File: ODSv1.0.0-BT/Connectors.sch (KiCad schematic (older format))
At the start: 2 parts, among them J1 Conn_02x60_Odd_Even, J2 Conn_02x60_Odd_Even

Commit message: Associate backplane template symbols with footprints and BOM info
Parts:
- J1: MPN (none) -> FX20-120P-0.5SV15; Manufacturer (none) -> Hirose; Ordering URL (none) -> https://www.digikey.com/en/products/detail/hirose-electric-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
- J2: footprint Backplane_Connector_Hirose:Hirose_FX20_FX20-120P-0.5SV_2x60_P0.50mm_Vertical -> Backplane_Connector_Hirose:Hirose_FX20_FX20-120S-0.5SV_2x60_P0.50mm_Vertical; MPN (none) -> FX20-120S-0.5SV; Manufacturer (none) -> Hirose; Ordering URL (none) -> https://www.digikey.com/en/products/detail/hirose-electric-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
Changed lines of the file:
@@
 F 2 "Backplane_Connector_Hirose:Hirose_FX20_FX20-120P-0.5SV_2x60_P0.50mm_Vertical" H 2450 3950 50  0001 C CNN
 F 3 "https://www.hirose.com/product/document?clcode=&productname=&series=FX20&documenttype=Catalog&lang=en&documentid=D49373_en" H 2450 3950 50  0001 C CNN
+F 4 "FX20-120P-0.5SV15" H 2450 3950 50  0001 C CNN "MPN"
+F 5 "Hirose" H 2450 3950 50  0001 C CNN "Manufacturer"
+F 6 "https://www.digikey.com/en/products/detail/hirose-electric-co-ltd/FX20-120P-0-5SV15/3461671" H 2450 3950 50  0001 C CNN "Ordering URL"
 	1    2450 3950
 	1    0    0    -1
@@
 F 0 "J2" H 5500 7067 50  0000 C CNN
 F 1 "Conn_02x60_Odd_Even" H 5500 6976 50  0000 C CNN
-F 2 "Backplane_Connector_Hirose:Hirose_FX20_FX20-120P-0.5SV_2x60_P0.50mm_Vertical" H 5450 3950 50  0001 C CNN
+F 2 "Backplane_Connector_Hirose:Hirose_FX20_FX20-120S-0.5SV_2x60_P0.50mm_Vertical" H 5450 3950 50  0001 C CNN
 F 3 "https://www.hirose.com/product/document?clcode=&productname=&series=FX20&documenttype=Catalog&lang=en&documentid=D49373_en" H 5450 3950 50  0001 C CNN
+F 4 "FX20-120S-0.5SV" H 5450 3950 50  0001 C CNN "MPN"
+F 5 "Hirose" H 5450 3950 50  0001 C CNN "Manufacturer"
+F 6 "https://www.digikey.com/en/products/detail/hirose-electric-co-ltd/FX20-120S-0-5SV/3461673" H 5450 3950 50  0001 C CNN "Ordering URL"
 	1    5450 3950
 	1    0    0    -1

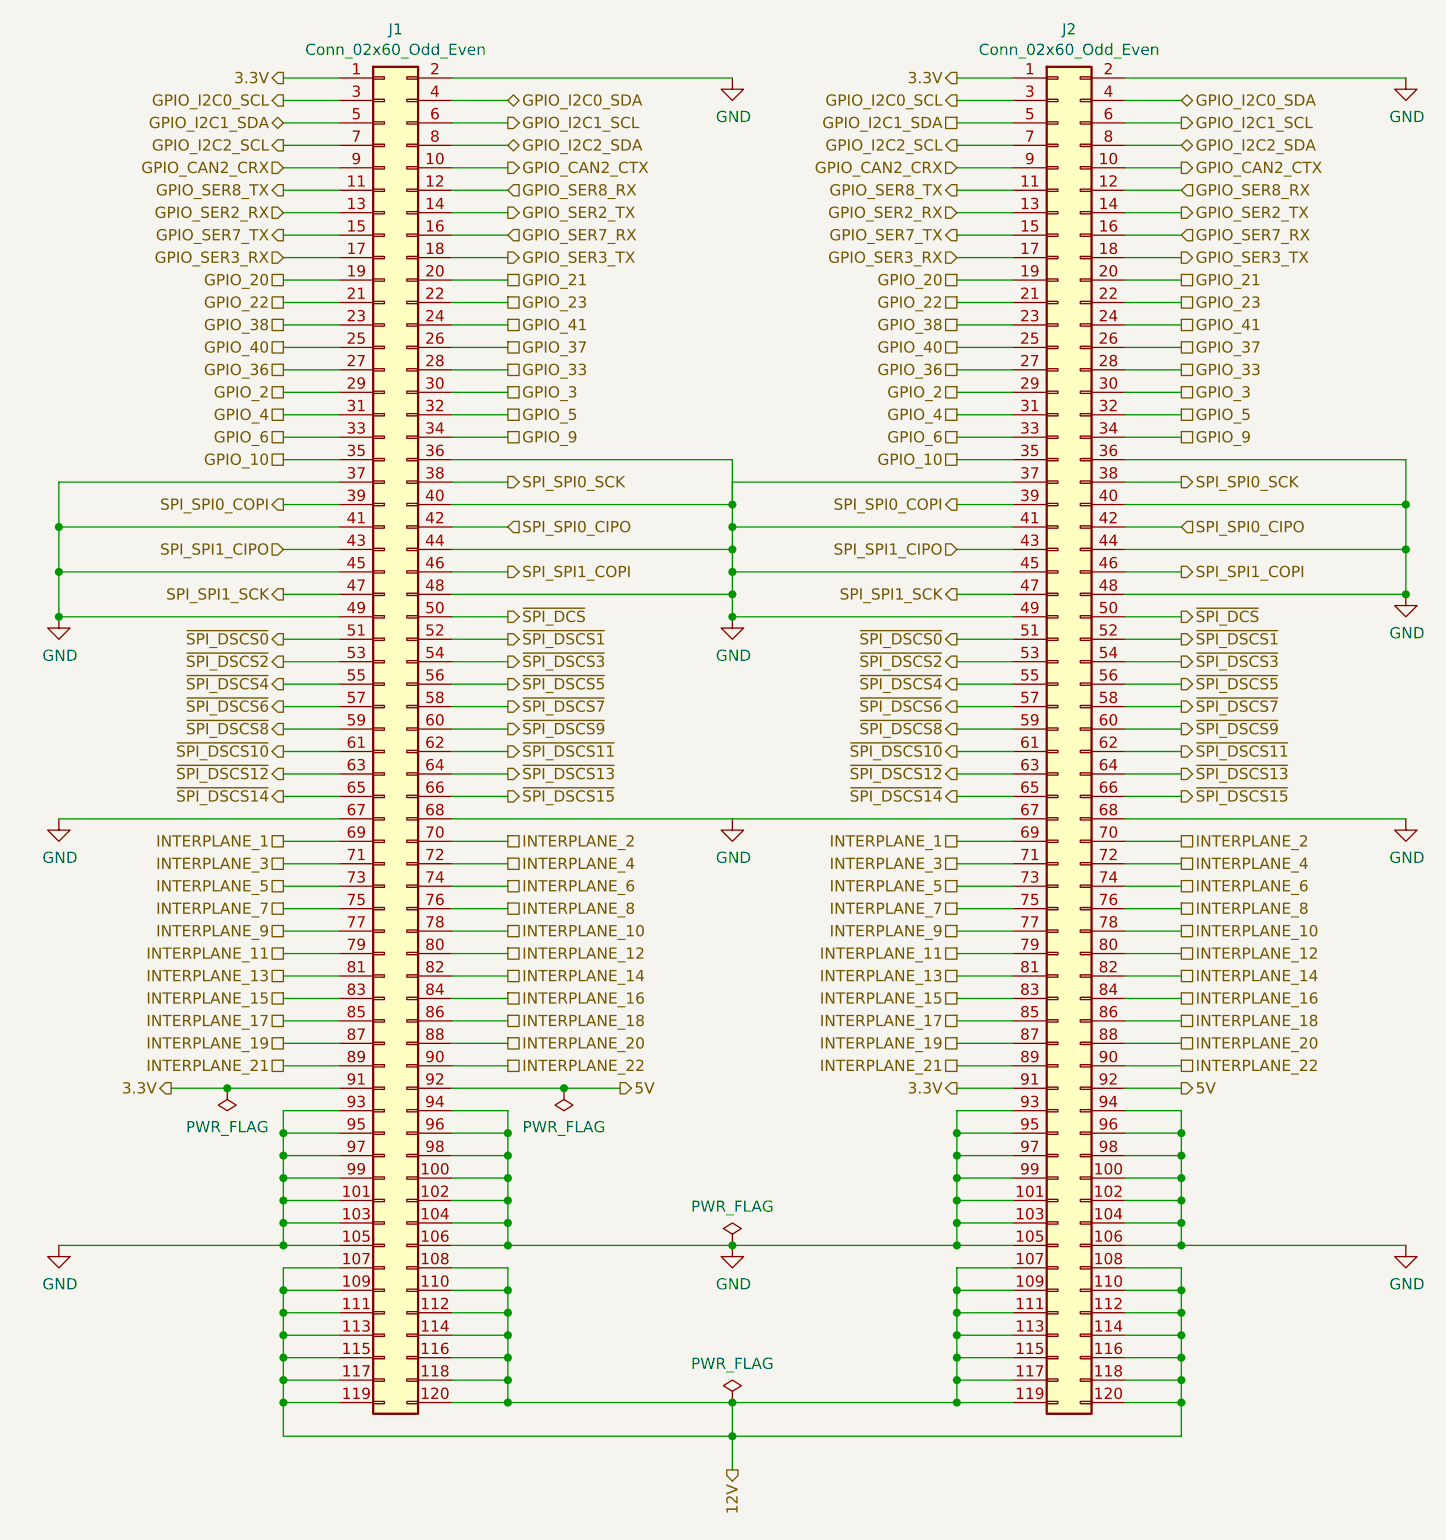
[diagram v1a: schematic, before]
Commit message: Remap pins for easier layout
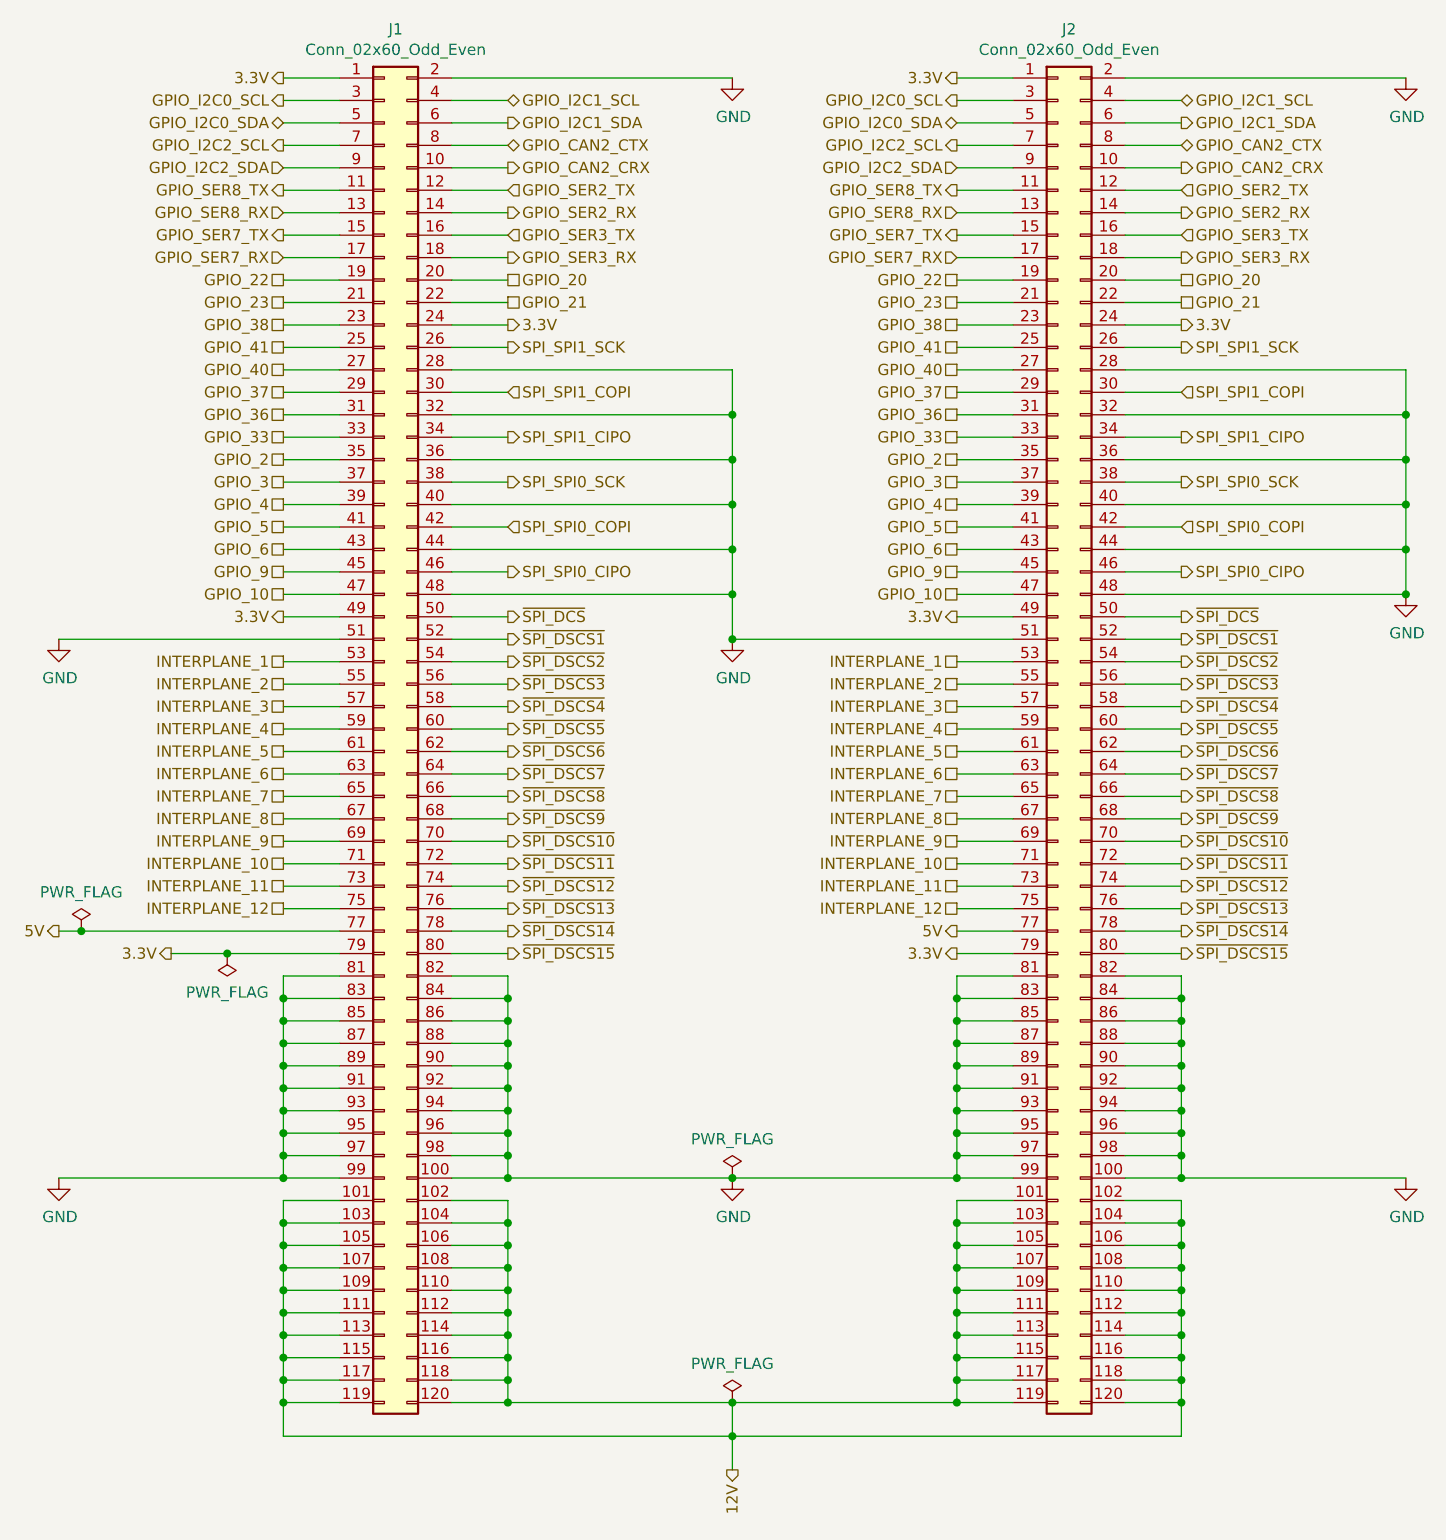
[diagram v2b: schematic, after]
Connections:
- net INTERPLANE_13 is gone; now on net GND: J1.81 (Pin_81), J2.81 (Pin_81)
- net INTERPLANE_14 is gone; now on net GND: J1.82 (Pin_82), J2.82 (Pin_82)
- net INTERPLANE_15 is gone; now on net GND: J1.83 (Pin_83), J2.83 (Pin_83)
- net INTERPLANE_16 is gone; now on net GND: J1.84 (Pin_84), J2.84 (Pin_84)
- net INTERPLANE_17 is gone; now on net GND: J1.85 (Pin_85), J2.85 (Pin_85)
- net INTERPLANE_18 is gone; now on net GND: J1.86 (Pin_86), J2.86 (Pin_86)
- net INTERPLANE_19 is gone; now on net GND: J1.87 (Pin_87), J2.87 (Pin_87)
- net INTERPLANE_20 is gone; now on net GND: J1.88 (Pin_88), J2.88 (Pin_88)
- net INTERPLANE_21 is gone; now on net GND: J1.89 (Pin_89), J2.89 (Pin_89)
- net INTERPLANE_22 is gone; now on net GND: J1.90 (Pin_90), J2.90 (Pin_90)
- net ~SPI_DSCS0~ is gone; now on net GND: J1.51 (Pin_51), J2.51 (Pin_51)
- net 12V: now also J1.101 (Pin_101), J1.102 (Pin_102), J1.103 (Pin_103), J1.104 (Pin_104), J1.105 (Pin_105), J1.106 (Pin_106), J2.101 (Pin_101), J2.102 (Pin_102), J2.103 (Pin_103), J2.104 (Pin_104), J2.105 (Pin_105), J2.106 (Pin_106)
- net 3.3V: now also J1.24 (Pin_24), J1.49 (Pin_49), J1.79 (Pin_79), J2.24 (Pin_24), J2.49 (Pin_49), J2.79 (Pin_79); no longer J1.91 (Pin_91), J2.91 (Pin_91)
- net 5V: now also J1.77 (Pin_77), J2.77 (Pin_77); no longer J1.92 (Pin_92), J2.92 (Pin_92)
- net GND: now also J1.28 (Pin_28), J1.32 (Pin_32), J1.91 (Pin_91), J1.92 (Pin_92), J2.28 (Pin_28), J2.32 (Pin_32), J2.91 (Pin_91), J2.92 (Pin_92); no longer J1.101 (Pin_101), J1.102 (Pin_102), J1.103 (Pin_103), J1.104 (Pin_104), J1.105 (Pin_105), J1.106 (Pin_106), J1.37 (Pin_37), J1.41 (Pin_41), J1.45 (Pin_45), J1.49 (Pin_49), J1.67 (Pin_67), J1.68 (Pin_68), J2.101 (Pin_101), J2.102 (Pin_102), J2.103 (Pin_103), J2.104 (Pin_104), J2.105 (Pin_105), J2.106 (Pin_106), J2.37 (Pin_37), J2.41 (Pin_41), J2.45 (Pin_45), J2.49 (Pin_49), J2.67 (Pin_67), J2.68 (Pin_68)
- net GPIO_10: now also J1.47 (Pin_47), J2.47 (Pin_47); no longer J1.35 (Pin_35), J2.35 (Pin_35)
- net GPIO_2: now also J1.35 (Pin_35), J2.35 (Pin_35); no longer J1.29 (Pin_29), J2.29 (Pin_29)
- net GPIO_20: now also J1.20 (Pin_20), J2.20 (Pin_20); no longer J1.19 (Pin_19), J2.19 (Pin_19)
- net GPIO_21: now also J1.22 (Pin_22), J2.22 (Pin_22); no longer J1.20 (Pin_20), J2.20 (Pin_20)
- net GPIO_22: now also J1.19 (Pin_19), J2.19 (Pin_19); no longer J1.21 (Pin_21), J2.21 (Pin_21)
- net GPIO_23: now also J1.21 (Pin_21), J2.21 (Pin_21); no longer J1.22 (Pin_22), J2.22 (Pin_22)
- net GPIO_3: now also J1.37 (Pin_37), J2.37 (Pin_37); no longer J1.30 (Pin_30), J2.30 (Pin_30)
- net GPIO_33: now also J1.33 (Pin_33), J2.33 (Pin_33); no longer J1.28 (Pin_28), J2.28 (Pin_28)
- net GPIO_36: now also J1.31 (Pin_31), J2.31 (Pin_31); no longer J1.27 (Pin_27), J2.27 (Pin_27)
- net GPIO_37: now also J1.29 (Pin_29), J2.29 (Pin_29); no longer J1.26 (Pin_26), J2.26 (Pin_26)
- net GPIO_4: now also J1.39 (Pin_39), J2.39 (Pin_39); no longer J1.31 (Pin_31), J2.31 (Pin_31)
- net GPIO_40: now also J1.27 (Pin_27), J2.27 (Pin_27); no longer J1.25 (Pin_25), J2.25 (Pin_25)
- net GPIO_41: now also J1.25 (Pin_25), J2.25 (Pin_25); no longer J1.24 (Pin_24), J2.24 (Pin_24)
- net GPIO_5: now also J1.41 (Pin_41), J2.41 (Pin_41); no longer J1.32 (Pin_32), J2.32 (Pin_32)
- net GPIO_6: now also J1.43 (Pin_43), J2.43 (Pin_43); no longer J1.33 (Pin_33), J2.33 (Pin_33)
- net GPIO_9: now also J1.45 (Pin_45), J2.45 (Pin_45); no longer J1.34 (Pin_34), J2.34 (Pin_34)
- net GPIO_CAN2_CRX: now also J1.10 (Pin_10), J2.10 (Pin_10); no longer J1.9 (Pin_9), J2.9 (Pin_9)
- net GPIO_CAN2_CTX: now also J1.8 (Pin_8), J2.8 (Pin_8); no longer J1.10 (Pin_10), J2.10 (Pin_10)
- net GPIO_I2C0_SDA: now also J1.5 (Pin_5), J2.5 (Pin_5); no longer J1.4 (Pin_4), J2.4 (Pin_4)
- net GPIO_I2C1_SCL: now also J1.4 (Pin_4), J2.4 (Pin_4); no longer J1.6 (Pin_6), J2.6 (Pin_6)
- net GPIO_I2C1_SDA: now also J1.6 (Pin_6), J2.6 (Pin_6); no longer J1.5 (Pin_5), J2.5 (Pin_5)
- net GPIO_I2C2_SDA: now also J1.9 (Pin_9), J2.9 (Pin_9); no longer J1.8 (Pin_8), J2.8 (Pin_8)
- net GPIO_SER2_RX: now also J1.14 (Pin_14), J2.14 (Pin_14); no longer J1.13 (Pin_13), J2.13 (Pin_13)
- net GPIO_SER2_TX: now also J1.12 (Pin_12), J2.12 (Pin_12); no longer J1.14 (Pin_14), J2.14 (Pin_14)
- net GPIO_SER3_RX: now also J1.18 (Pin_18), J2.18 (Pin_18); no longer J1.17 (Pin_17), J2.17 (Pin_17)
- net GPIO_SER3_TX: now also J1.16 (Pin_16), J2.16 (Pin_16); no longer J1.18 (Pin_18), J2.18 (Pin_18)
- net GPIO_SER7_RX: now also J1.17 (Pin_17), J2.17 (Pin_17); no longer J1.16 (Pin_16), J2.16 (Pin_16)
- net GPIO_SER8_RX: now also J1.13 (Pin_13), J2.13 (Pin_13); no longer J1.12 (Pin_12), J2.12 (Pin_12)
- net INTERPLANE_1: now also J1.53 (Pin_53), J2.53 (Pin_53); no longer J1.69 (Pin_69), J2.69 (Pin_69)
- net INTERPLANE_10: now also J1.71 (Pin_71), J2.71 (Pin_71); no longer J1.78 (Pin_78), J2.78 (Pin_78)
- net INTERPLANE_11: now also J1.73 (Pin_73), J2.73 (Pin_73); no longer J1.79 (Pin_79), J2.79 (Pin_79)
- net INTERPLANE_12: now also J1.75 (Pin_75), J2.75 (Pin_75); no longer J1.80 (Pin_80), J2.80 (Pin_80)
- net INTERPLANE_2: now also J1.55 (Pin_55), J2.55 (Pin_55); no longer J1.70 (Pin_70), J2.70 (Pin_70)
- net INTERPLANE_3: now also J1.57 (Pin_57), J2.57 (Pin_57); no longer J1.71 (Pin_71), J2.71 (Pin_71)
- net INTERPLANE_4: now also J1.59 (Pin_59), J2.59 (Pin_59); no longer J1.72 (Pin_72), J2.72 (Pin_72)
- net INTERPLANE_5: now also J1.61 (Pin_61), J2.61 (Pin_61); no longer J1.73 (Pin_73), J2.73 (Pin_73)
- net INTERPLANE_6: now also J1.63 (Pin_63), J2.63 (Pin_63); no longer J1.74 (Pin_74), J2.74 (Pin_74)
- net INTERPLANE_7: now also J1.65 (Pin_65), J2.65 (Pin_65); no longer J1.75 (Pin_75), J2.75 (Pin_75)
- net INTERPLANE_8: now also J1.67 (Pin_67), J2.67 (Pin_67); no longer J1.76 (Pin_76), J2.76 (Pin_76)
- net INTERPLANE_9: now also J1.69 (Pin_69), J2.69 (Pin_69); no longer J1.77 (Pin_77), J2.77 (Pin_77)
- net SPI_SPI0_CIPO: now also J1.46 (Pin_46), J2.46 (Pin_46); no longer J1.42 (Pin_42), J2.42 (Pin_42)
- net SPI_SPI0_COPI: now also J1.42 (Pin_42), J2.42 (Pin_42); no longer J1.39 (Pin_39), J2.39 (Pin_39)
- net SPI_SPI1_CIPO: now also J1.34 (Pin_34), J2.34 (Pin_34); no longer J1.43 (Pin_43), J2.43 (Pin_43)
- net SPI_SPI1_COPI: now also J1.30 (Pin_30), J2.30 (Pin_30); no longer J1.46 (Pin_46), J2.46 (Pin_46)
- net SPI_SPI1_SCK: now also J1.26 (Pin_26), J2.26 (Pin_26); no longer J1.47 (Pin_47), J2.47 (Pin_47)
- net ~SPI_DSCS10~: now also J1.70 (Pin_70), J2.70 (Pin_70); no longer J1.61 (Pin_61), J2.61 (Pin_61)
- net ~SPI_DSCS11~: now also J1.72 (Pin_72), J2.72 (Pin_72); no longer J1.62 (Pin_62), J2.62 (Pin_62)
- net ~SPI_DSCS12~: now also J1.74 (Pin_74), J2.74 (Pin_74); no longer J1.63 (Pin_63), J2.63 (Pin_63)
- net ~SPI_DSCS13~: now also J1.76 (Pin_76), J2.76 (Pin_76); no longer J1.64 (Pin_64), J2.64 (Pin_64)
- net ~SPI_DSCS14~: now also J1.78 (Pin_78), J2.78 (Pin_78); no longer J1.65 (Pin_65), J2.65 (Pin_65)
- net ~SPI_DSCS15~: now also J1.80 (Pin_80), J2.80 (Pin_80); no longer J1.66 (Pin_66), J2.66 (Pin_66)
- net ~SPI_DSCS2~: now also J1.54 (Pin_54), J2.54 (Pin_54); no longer J1.53 (Pin_53), J2.53 (Pin_53)
- net ~SPI_DSCS3~: now also J1.56 (Pin_56), J2.56 (Pin_56); no longer J1.54 (Pin_54), J2.54 (Pin_54)
- net ~SPI_DSCS4~: now also J1.58 (Pin_58), J2.58 (Pin_58); no longer J1.55 (Pin_55), J2.55 (Pin_55)
- net ~SPI_DSCS5~: now also J1.60 (Pin_60), J2.60 (Pin_60); no longer J1.56 (Pin_56), J2.56 (Pin_56)
- net ~SPI_DSCS6~: now also J1.62 (Pin_62), J2.62 (Pin_62); no longer J1.57 (Pin_57), J2.57 (Pin_57)
- net ~SPI_DSCS7~: now also J1.64 (Pin_64), J2.64 (Pin_64); no longer J1.58 (Pin_58), J2.58 (Pin_58)
- net ~SPI_DSCS8~: now also J1.66 (Pin_66), J2.66 (Pin_66); no longer J1.59 (Pin_59), J2.59 (Pin_59)
- net ~SPI_DSCS9~: now also J1.68 (Pin_68), J2.68 (Pin_68); no longer J1.60 (Pin_60), J2.60 (Pin_60)
